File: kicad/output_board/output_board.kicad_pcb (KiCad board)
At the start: 2 copper layers, 109.2 x 48.3 mm, 88 parts, among them J1 DRV_PWR, J2 DRV, J3 CH_OUT, Q1 IRF9Z24NPBF, Q10 IRF9Z24NPBF, Q11 AO3400A, Q12 AO3400A, Q2 AO3400A, Q3 AO3400A, Q4 IRF9Z24NPBF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

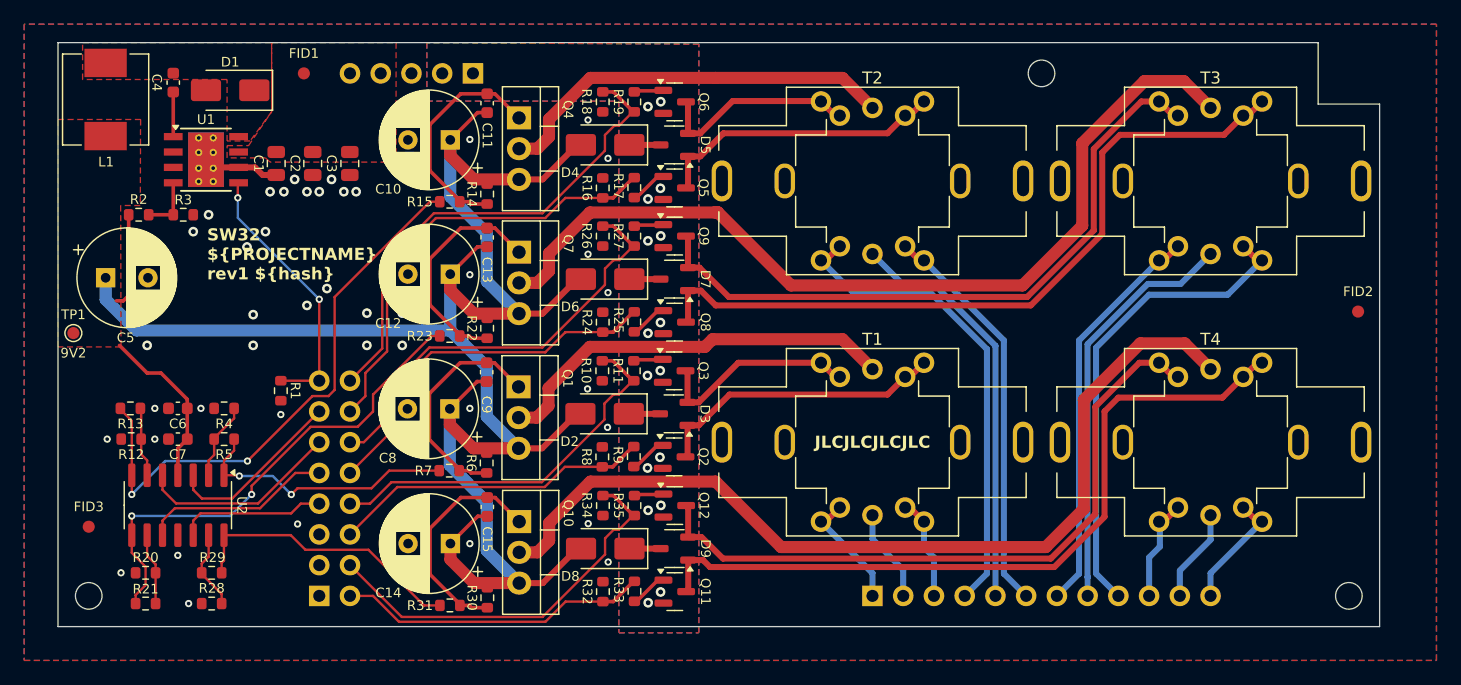
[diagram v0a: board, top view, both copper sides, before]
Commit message: unify via sizes
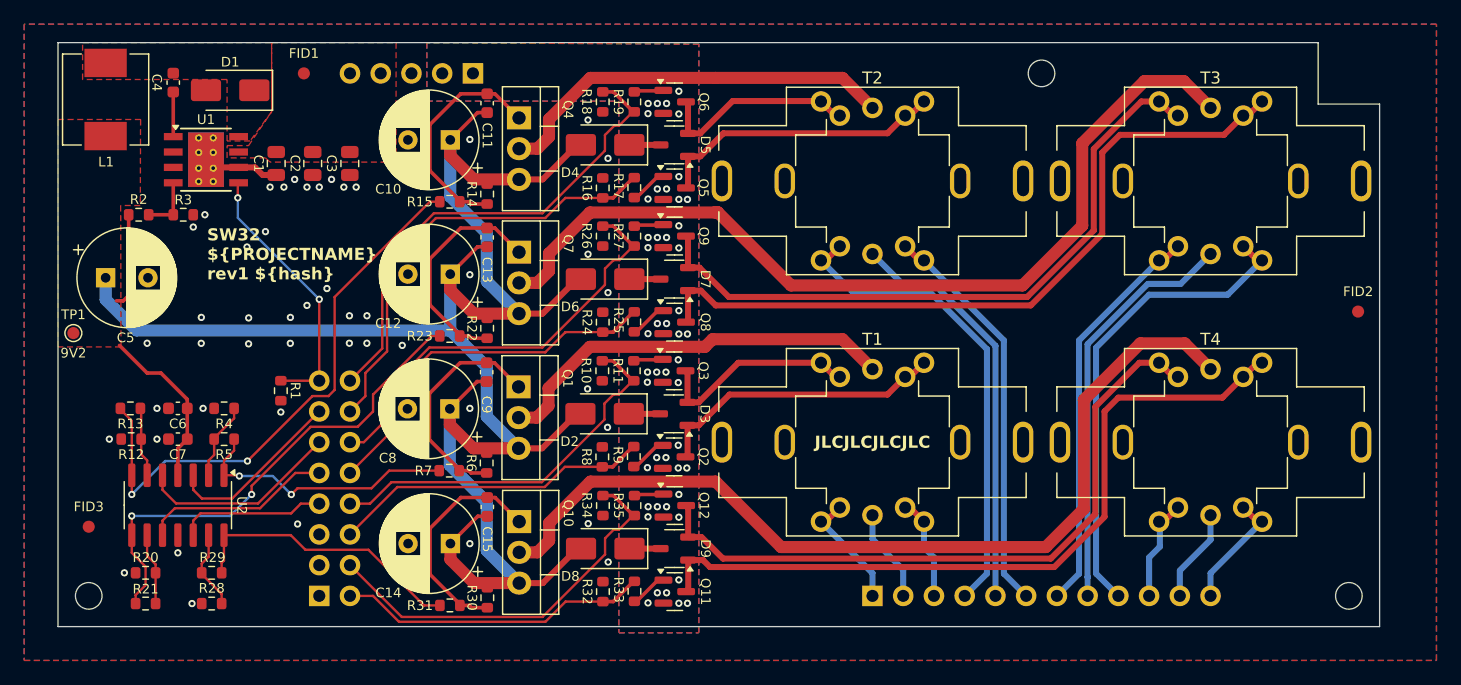
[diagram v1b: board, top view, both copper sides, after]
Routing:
- net GND: vias 43 -> 49
- net /PGND: vias 16 -> 48

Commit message: fix title block
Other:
- board text added: "${TITLE} ${PROJECTNAME} rev${REVISION} ${hash}"
- board text removed: "SW32 ${PROJECTNAME} rev${REVISION} ${hash}"
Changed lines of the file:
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@@
 	(paper "A4")
 	(title_block
-		(title "SW32 - Output Board")
+		(title "SW32")
 		(date "2024-06-10")
 		(rev "1")
@@
 		)
 	)
-	(gr_text "SW32\n${PROJECTNAME}\nrev${REVISION} ${hash}"
+	(gr_text "${TITLE}\n${PROJECTNAME}\nrev${REVISION} ${hash}"
 		(locked yes)
 		(at 115.316032 91.674197 0)

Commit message: add plot settings
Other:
- board text added: "${TITLE} ${PROJECTNAME} rev${REVISION}"
- board text removed: "${TITLE} ${PROJECTNAME} rev${REVISION} ${hash}"
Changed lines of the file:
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@@
 	(title_block
 		(title "SW32")
-		(date "2024-06-10")
+		(date "2024-06-12")
 		(rev "1")
 		(company "saawsm")
@@
 			(plot_on_all_layers_selection 0x0000000_00000000)
 			(disableapertmacros no)
-			(usegerberextensions no)
-			(usegerberattributes yes)
-			(usegerberadvancedattributes yes)
-			(creategerberjobfile yes)
+			(usegerberextensions yes)
+			(usegerberattributes no)
+			(usegerberadvancedattributes no)
+			(creategerberjobfile no)
 			(dashed_line_dash_ratio 12.000000)
 			(dashed_line_gap_ratio 3.000000)
@@
 			(plotinvisibletext no)
 			(sketchpadsonfab no)
-			(subtractmaskfromsilk no)
+			(subtractmaskfromsilk yes)
 			(outputformat 1)
 			(mirror no)
-			(drillshape 1)
+			(drillshape 0)
 			(scaleselection 1)
-			(outputdirectory "")
+			(outputdirectory "../../pcb/output_board/")
 		)
 	)
@@
 		)
 	)
-	(gr_text "${TITLE}\n${PROJECTNAME}\nrev${REVISION} ${hash}"
+	(gr_text "${TITLE}\n${PROJECTNAME}\nrev${REVISION}"
 		(locked yes)
 		(at 115.316032 91.674197 0)
